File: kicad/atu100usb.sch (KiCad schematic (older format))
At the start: 17 parts, among them J1 Conn_01x01_Shielded, J2 Conn_01x01_Shielded, J3 Conn_01x01_Shielded, J4 Conn_01x01_Shielded, K1 V23105A5476A201, K2 V23105A5476A201, Q1 2N3904, Q2 2N3904

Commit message: Updated the schematic.
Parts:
- added D1, D2, D3: LED, symbol Device:LED
- added R10, R6: 47K, symbol Device:R_Small_US
- added R11: 150K, symbol Device:R_Small_US
- added R3, R4, R5: 90, symbol Device:R_Small_US
- added R7: 9.1K, symbol Device:R_Small_US
- added R8: 15K, symbol Device:R_Small_US
- added R9: 24K, symbol Device:R_Small_US
- added SW1, SW2, SW3, SW4, SW5, SW6: SW_SPST, symbol Switch:SW_SPST
- added U?: PIC18F25K20_ISS, Package_SO:SSOP-28_5.3x10.2mm_P0.65mm, symbol MCU_Microchip_PIC18:PIC18F25K20_ISS
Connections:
- net GND: now also D1.1 (K), D2.1 (K), D3.1 (K), SW1.2 (B), SW2.2 (B), SW3.2 (B), SW4.2 (B), SW5.2 (B), SW6.2 (B)
- net at A?.13 (D10): now also R5.2
- net at A?.14 (D11): now also R4.2
- net at A?.15 (D12): now also R3.2
- net at A?.19 (A0): now also U?.9 (RA7/OSC1/CLKIN)
- net at A?.20 (A1): now also U?.23 (AN8/INT2/RB2)
- net at A?.21 (A2): now also U?.22 (AN10/INT1/RB1)
- net at A?.22 (A3): now also U?.21 (AN12/INT0/RB0)
- net at A?.23 (A4): now also U?.15 (SDA/SDI/RC4)
- net at A?.24 (A5): now also U?.14 (SCL/SCK/RC3)
- net at A?.25 (A6): now also R6.2
- new net: D1.2 (A), R3.1
- new net: D2.2 (A), R4.1
- new net: D3.2 (A), R5.1
- new net: R11.1, SW6.1 (A)
- new net: R10.1, R11.2, SW5.1 (A)
- new net: R10.2, R9.1, SW4.1 (A)
- new net: R8.1, R9.2, SW3.1 (A)
- new net: R7.1, R8.2, SW2.1 (A)
- new net: R6.1, R7.2, SW1.1 (A)
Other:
- note added: "ANT1"
- note added: "ANT2"
- note added: "AUTO"
- note added: "BYP"
- note added: "DL"
- note added: "TUNE"
- note added: "TX_req"
- note added: "Transceiver"
- moved on the sheet: A?

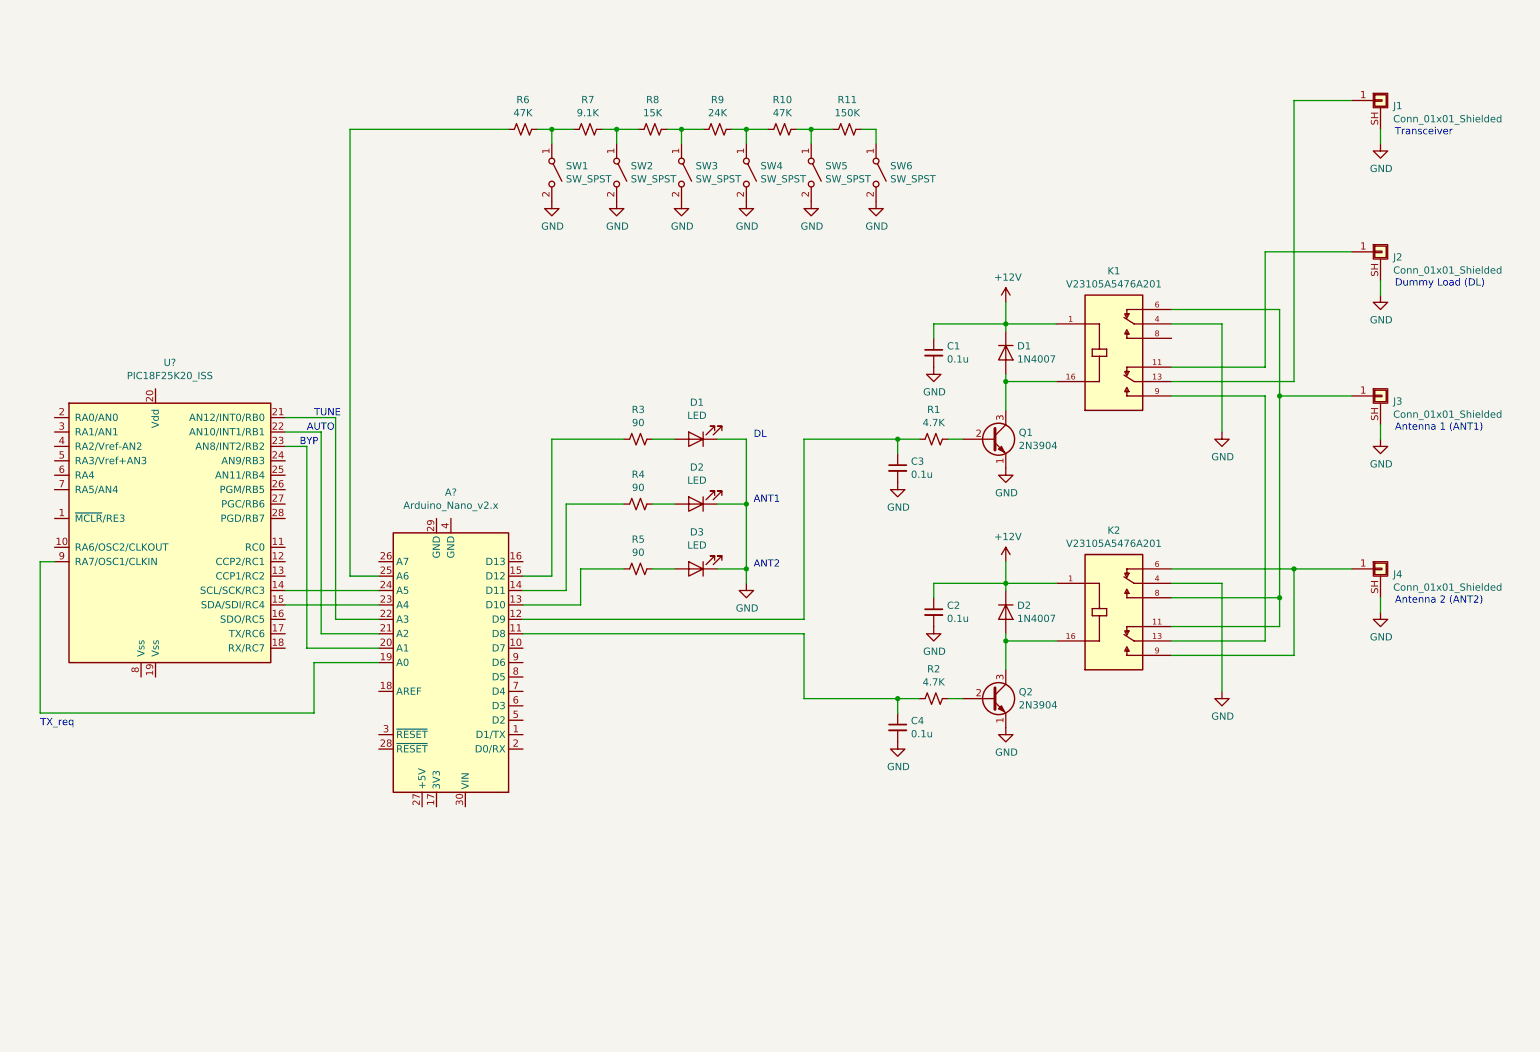
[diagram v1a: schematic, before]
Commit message: Updates.  Still need to fix the schematic... need three digital control lines for relays, and then also need to reduce LEDs to 3 lines via shift register (74HC595).
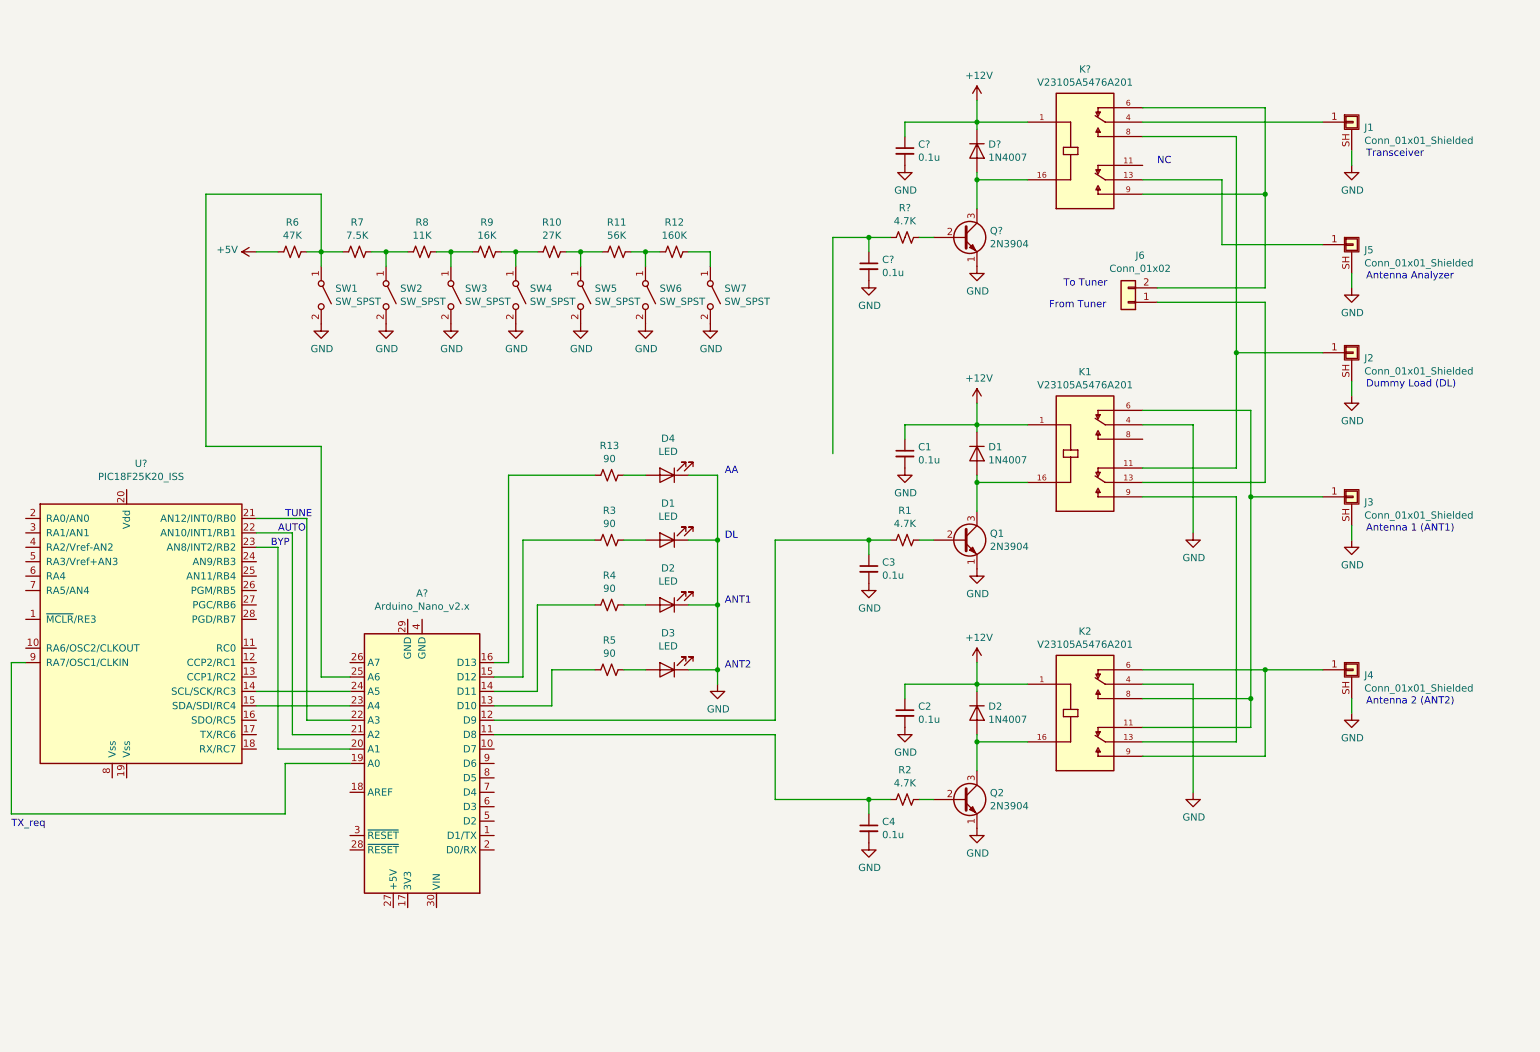
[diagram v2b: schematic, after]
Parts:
- added C? (x2): 0.1u, symbol Device:C_Small
- added D4: LED, symbol Device:LED
- added D?: 1N4007, Diode_THT:D_DO-41_SOD81_P10.16mm_Horizontal, symbol Diode:1N4007
- added J5: Conn_01x01_Shielded, symbol Connector_Generic_Shielded:Conn_01x01_Shielded
- added J6: Conn_01x02, symbol Connector_Generic:Conn_01x02
- added K?: V23105A5476A201, RELAY_9-1393792-3, symbol V23105A5301A201:V23105A5301A201
- added Q?: 2N3904, Package_TO_SOT_THT:TO-92_Inline, symbol Transistor_BJT:2N3904
- added R12: 160K, symbol Device:R_Small_US
- added R13: 90, symbol Device:R_Small_US
- added R?: 4.7K, symbol Device:R_Small_US
- added SW7: SW_SPST, symbol Switch:SW_SPST
- R10: value 47K -> 27K
- R11: value 150K -> 56K
- R7: value 9.1K -> 7.5K
- R8: value 15K -> 11K
- R9: value 24K -> 16K
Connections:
- net +12V: now also C?.1, D?.1 (K), K?.1
- net GND: now also C?.2, C?.2, D4.1 (K), J5.SH (Shield), Q?.1 (E), SW7.2 (B)
- net at J2.1 (Pin_1), K1.11: now also K?.8
- net at K1.13: now also J6.1 (Pin_1); no longer J1.1 (Pin_1)
- net at A?.16 (D13): now also R13.2
- net at A?.25 (A6): now also R6.1, R7.2, SW1.1 (A); no longer R6.2
- net at R11.1, SW6.1 (A): now also R12.2
- new net: J1.1 (Pin_1), K?.4
- new net: J5.1 (Pin_1), K?.13
- new net: D?.2 (A), K?.16, Q?.3 (C)
- new net: J6.2 (Pin_2), K?.6, K?.9
- new net: D4.2 (A), R13.1
- new net: R12.1, SW7.1 (A)
- new net: Q?.2 (B), R?.1
- new net: C?.1, R?.2
- new net +5V: R6.2
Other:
- note added: "AA"
- note added: "Antenna Analyzer"
- note added: "From Tuner"
- note added: "NC"
- note added: "To Tuner"
- moved on the sheet: A?, C1, C2, C3, C4, D1, D2, D3, J1, J2, J3, J4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

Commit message: some updates
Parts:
- gave numbers to parts that had none: 5
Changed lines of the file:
@@
 Dummy Load (DL)
-Wire Wire Line
-	8600 3700 9250 3700
-Wire Wire Line
-	9250 3700 9250 2900
-Wire Wire Line
-	9250 2900 9850 2900
 Wire Wire Line
 	8600 3900 9250 3900
@@
 	9450 1200 9450 1800
 Wire Wire Line
-	8600 1400 9250 1400
-Wire Wire Line
-	9250 1400 9250 2900
-Connection ~ 9250 2900
-Wire Wire Line
 	8600 1800 9450 1800
 Text Notes 8700 1600 0    50   ~ 0
@@
 Text Notes 5700 3750 0    50   ~ 0
 AA
-Connection ~ 9450 1800
-Wire Wire Line
-	9450 1800 9450 2450
 $Comp
 L Connector_Generic:Conn_01x02 J6
@@
 	2100 1800 2900 1800
 $Comp
-L Transistor_BJT:2N3904 Q?
+L Transistor_BJT:2N3904 Q3
 U 1 1 627419CF
 P 7350 2100
-F 0 "Q?" H 7540 2146 50  0000 L CNN
+F 0 "Q3" H 7540 2146 50  0000 L CNN
 F 1 "2N3904" H 7540 2055 50  0000 L CNN
 F 2 "Package_TO_SOT_THT:TO-92_Inline" H 7550 2025 50  0001 L CIN
@@
 $EndComp
 $Comp
-L Diode:1N4007 D?
+L Diode:1N4007 D3
 U 1 1 627419D5
 P 7450 1500
-F 0 "D?" V 7404 1579 50  0000 L CNN
+F 0 "D3" V 7404 1579 50  0000 L CNN
 F 1 "1N4007" V 7495 1579 50  0000 L CNN
 F 2 "Diode_THT:D_DO-41_SOD81_P10.16mm_Horizontal" H 7450 1325 50  0001 C CNN
@@
 $EndComp
 $Comp
-L Device:C_Small C?
+L Device:C_Small C4
 U 1 1 627419E1
 P 6950 1500
-F 0 "C?" H 7042 1546 50  0000 L CNN
+F 0 "C4" H 7042 1546 50  0000 L CNN
 F 1 "0.1u" H 7042 1455 50  0000 L CNN
 F 2 "" H 6950 1500 50  0001 C CNN
@@
 Connection ~ 7450 1700
 $Comp
-L Device:R_Small_US R?
+L Device:R_Small_US R14
 U 1 1 627419F6
 P 6950 2100
-F 0 "R?" V 6745 2100 50  0000 C CNN
+F 0 "R14" V 6745 2100 50  0000 C CNN
 F 1 "4.7K" V 6836 2100 50  0000 C CNN
 F 2 "" H 6950 2100 50  0001 C CNN
@@
 	7050 2100 7150 2100
 $Comp
-L Device:C_Small C?
+L Device:C_Small C5
 U 1 1 62741A04
 P 6700 2300
-F 0 "C?" H 6792 2346 50  0000 L CNN
+F 0 "C5" H 6792 2346 50  0000 L CNN
 F 1 "0.1u" H 6792 2255 50  0000 L CNN
 F 2 "" H 6700 2300 50  0001 C CNN
@@
 	6450 2100 6450 3600
 Connection ~ 6700 2100
+Connection ~ 9450 1800
+Wire Wire Line
+	9450 1800 9450 2450
+Wire Wire Line
+	9550 1400 9550 2900
+Connection ~ 9550 2900
+Wire Wire Line
+	9550 2900 9850 2900
+Wire Wire Line
+	8600 1400 9550 1400
+Wire Wire Line
+	9550 2900 9550 3700
+Wire Wire Line
+	8600 3700 9550 3700
 $EndSCHEMATC

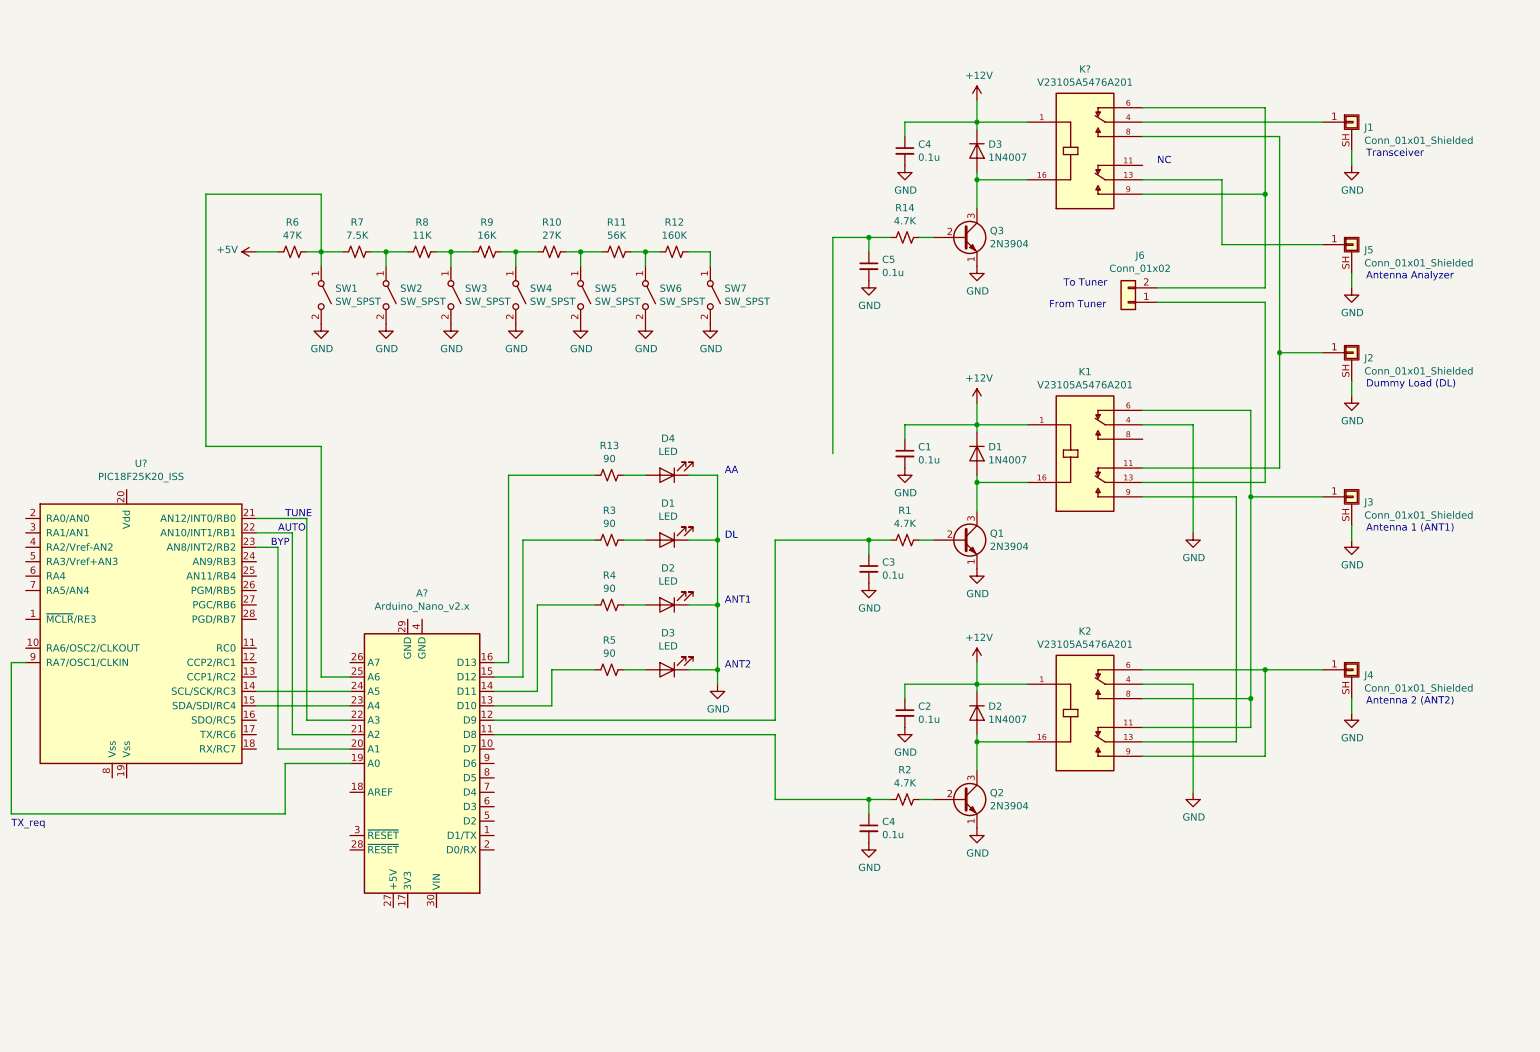
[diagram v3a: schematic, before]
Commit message: Fixed numbering on schematic.
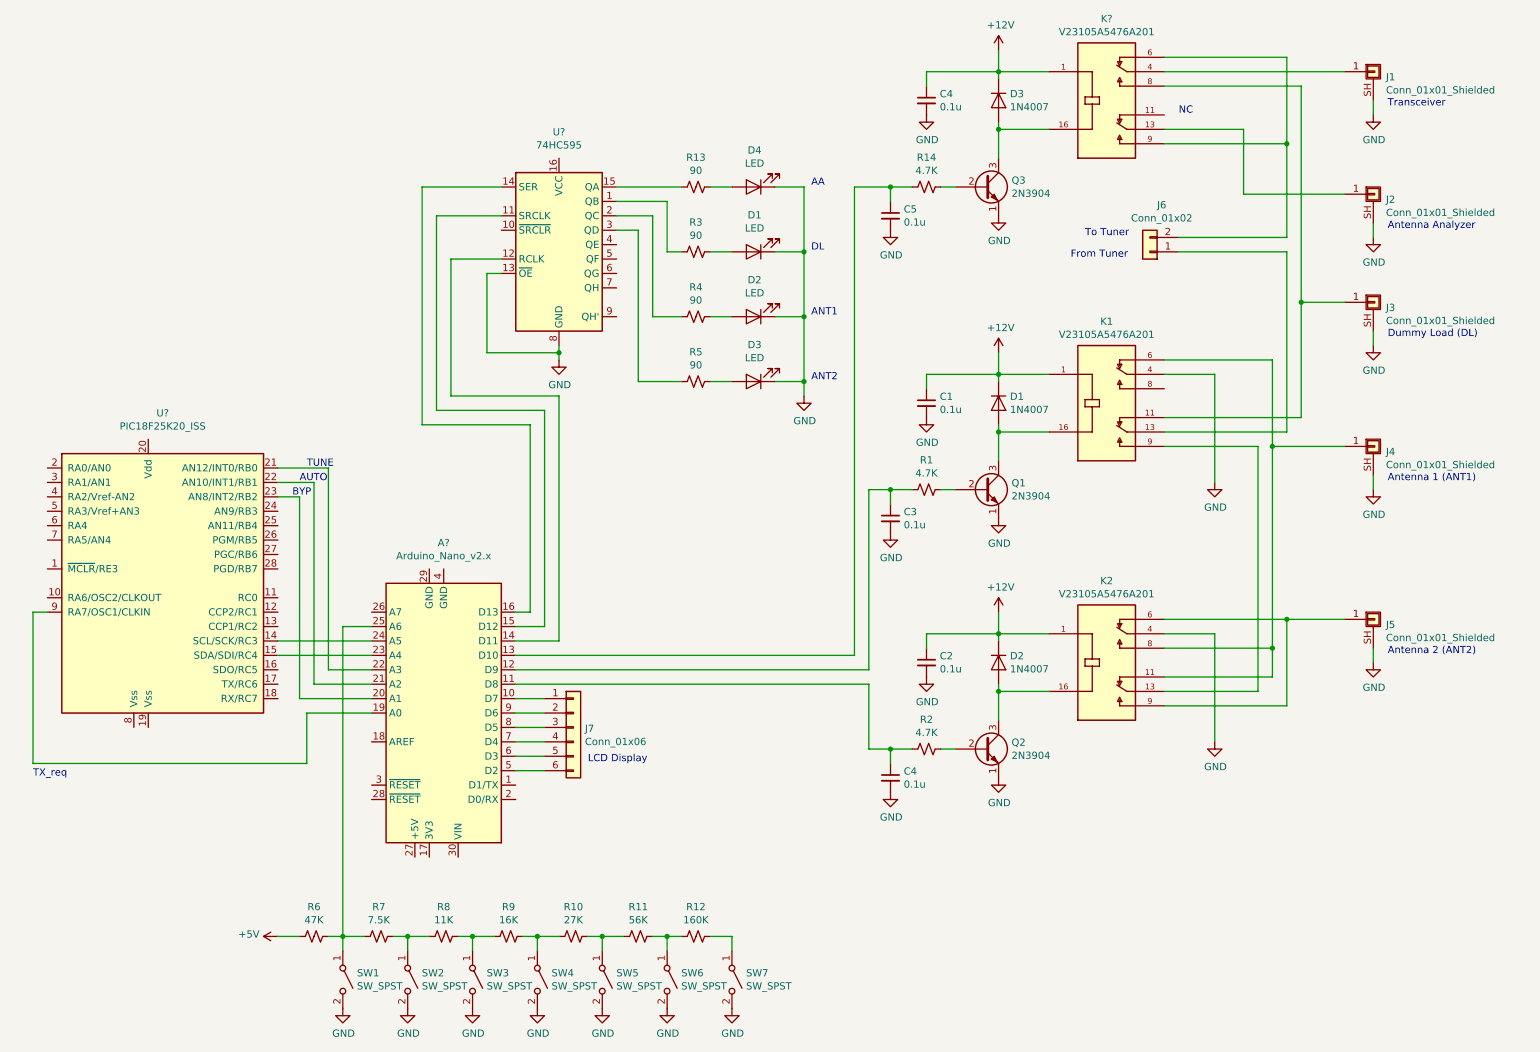
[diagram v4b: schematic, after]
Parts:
- added J7: Conn_01x06, symbol Connector_Generic:Conn_01x06
- added U?: 74HC595, symbol 74xx:74HC595
- renumbered J5 to J2, J2 to J3, J3 to J4, J4 to J5
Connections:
- net GND: now also U?.13 (~OE), U?.8 (GND)
- net at A?.10 (D7): now also J7.1 (Pin_1)
- net at A?.13 (D10): now also C5.1, R14.2; no longer R5.2
- net at A?.14 (D11): now also U?.12 (RCLK); no longer R4.2
- net at A?.15 (D12): now also U?.11 (SRCLK); no longer R3.2
- net at A?.16 (D13): now also U?.14 (SER); no longer R13.2
- net at A?.5 (D2): now also J7.6 (Pin_6)
- net at A?.6 (D3): now also J7.5 (Pin_5)
- net at A?.7 (D4): now also J7.4 (Pin_4)
- net at A?.8 (D5): now also J7.3 (Pin_3)
- net at A?.9 (D6): now also J7.2 (Pin_2)
- new net: R3.2, U?.1 (QB)
- new net: R4.2, U?.2 (QC)
- new net: R5.2, U?.3 (QD)
- new net: R13.2, U?.15 (QA)
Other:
- note added: "LCD Display"
- moved on the sheet: A?, C1, C2, C3, C4, C5, D1, D2, D3, D4, J1, J2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
